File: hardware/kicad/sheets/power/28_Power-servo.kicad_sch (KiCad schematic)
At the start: 18 parts, among them U37 TPSM63610RDFR

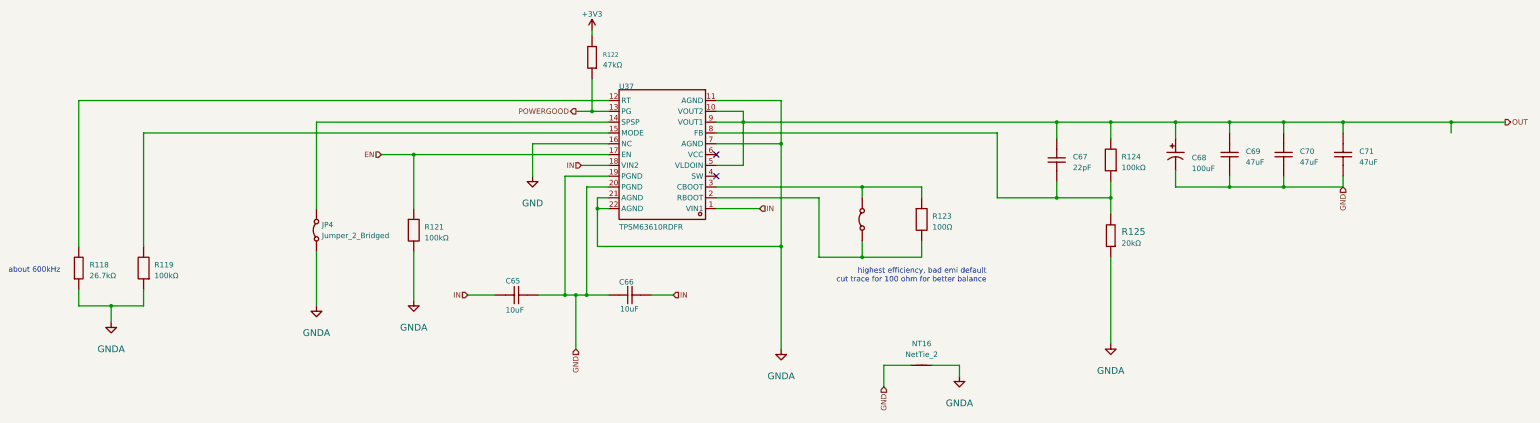
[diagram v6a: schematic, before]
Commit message: 5v usb c done, esc mostly done
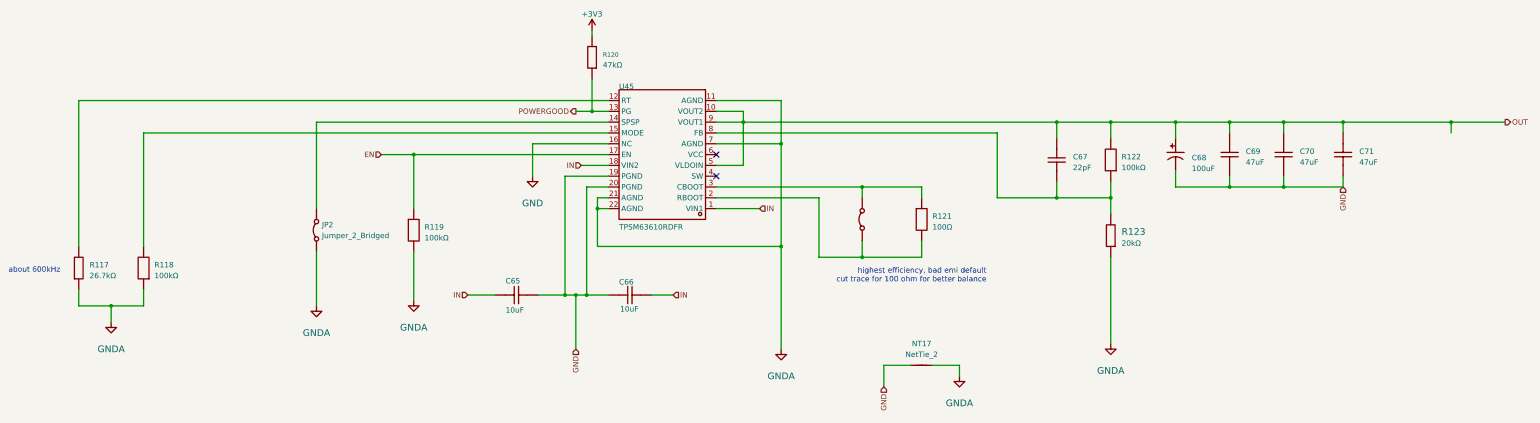
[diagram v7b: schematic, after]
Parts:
- renumbered JP4 to JP2, NT16 to NT17, R118 to R117, R119 to R118, R121 to R119, R122 to R120, R123 to R121, R124 to R122, R125 to R123, U37 to U45, U38 to U46
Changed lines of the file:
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@@
 		(dnp no)
 		(fields_autoplaced yes)
-		(property "Reference" "JP4"
+		(property "Reference" "JP2"
 			(at 93.98 109.2199 90)
 			(effects
@@
 			(project ""
 				(path "/3f85abf4-0b95-4c4a-b7e9-06f59ca1ea3d/5c2e021f-c2d4-49e2-8c36-9a64f1f12001/5e87fa27-0735-4860-928c-5f9d8795dad6"
-					(reference "JP4")
+					(reference "JP2")
 					(unit 1)
 				)
@@
 		(on_board yes)
 		(dnp no)
-		(property "Reference" "R125"
+		(property "Reference" "R123"
 			(at 281.94 111.76 90)
 			(effects
@@
 			(project "svea_powerboard_rev3"
 				(path "/3f85abf4-0b95-4c4a-b7e9-06f59ca1ea3d/5c2e021f-c2d4-49e2-8c36-9a64f1f12001/5e87fa27-0735-4860-928c-5f9d8795dad6"
-					(reference "R125")
+					(reference "R123")
 					(unit 1)
 				)
@@
 		(on_board yes)
 		(dnp no)
-		(property "Reference" "U38"
+		(property "Reference" "U46"
 			(at 220.98 107.95 90)
 			(effects
@@
 			(project "svea_powerboard_rev3"
 				(path "/3f85abf4-0b95-4c4a-b7e9-06f59ca1ea3d/5c2e021f-c2d4-49e2-8c36-9a64f1f12001/5e87fa27-0735-4860-928c-5f9d8795dad6"
-					(reference "U38")
+					(reference "U46")
 					(unit 1)
 				)
@@
 		(on_board yes)
 		(dnp no)
-		(property "Reference" "#PWR0112"
+		(property "Reference" "#PWR0110"
 			(at 243.84 144.78 0)
 			(effects
@@
 			(project "svea_powerboard_rev3"
 				(path "/3f85abf4-0b95-4c4a-b7e9-06f59ca1ea3d/5c2e021f-c2d4-49e2-8c36-9a64f1f12001/5e87fa27-0735-4860-928c-5f9d8795dad6"
-					(reference "#PWR0112")
+					(reference "#PWR0110")
 					(unit 1)
 				)
@@
 		(dnp no)
 		(fields_autoplaced yes)
-		(property "Reference" "NT16"
+		(property "Reference" "NT17"
 			(at 234.95 137.16 0)
 			(effects
@@
 			(project "svea_powerboard_rev3"
 				(path "/3f85abf4-0b95-4c4a-b7e9-06f59ca1ea3d/5c2e021f-c2d4-49e2-8c36-9a64f1f12001/5e87fa27-0735-4860-928c-5f9d8795dad6"
-					(reference "NT16")
+					(reference "NT17")
 					(unit 1)
 				)
@@
 		(on_board yes)
 		(dnp no)
-		(property "Reference" "R124"
+		(property "Reference" "R122"
 			(at 281.94 93.98 90)
 			(effects
@@
 			(project "svea_powerboard_rev3"
 				(path "/3f85abf4-0b95-4c4a-b7e9-06f59ca1ea3d/5c2e021f-c2d4-49e2-8c36-9a64f1f12001/5e87fa27-0735-4860-928c-5f9d8795dad6"
-					(reference "R124")
+					(reference "R122")
 					(unit 1)
 				)
@@
 		(on_board yes)
 		(dnp no)
-		(property "Reference" "#PWR0106"
+		(property "Reference" "#PWR0104"
 			(at 44.45 132.08 0)
 			(effects
@@
 			(project "svea_powerboard_rev3"
 				(path "/3f85abf4-0b95-4c4a-b7e9-06f59ca1ea3d/5c2e021f-c2d4-49e2-8c36-9a64f1f12001/5e87fa27-0735-4860-928c-5f9d8795dad6"
-					(reference "#PWR0106")
+					(reference "#PWR0104")
 					(unit 1)
 				)
@@
 		(on_board yes)
 		(dnp no)
-		(property "Reference" "#PWR0113"
+		(property "Reference" "#PWR0111"
 			(at 279.4 137.16 0)
 			(effects
@@
 			(project "svea_powerboard_rev3"
 				(path "/3f85abf4-0b95-4c4a-b7e9-06f59ca1ea3d/5c2e021f-c2d4-49e2-8c36-9a64f1f12001/5e87fa27-0735-4860-928c-5f9d8795dad6"
-					(reference "#PWR0113")
+					(reference "#PWR0111")
 					(unit 1)
 				)
@@
 		(on_board yes)
 		(dnp no)
-		(property "Reference" "R118"
+		(property "Reference" "R117"
 			(at 39.37 119.38 90)
 			(effects
@@
 			(project "svea_powerboard_rev3"
 				(path "/3f85abf4-0b95-4c4a-b7e9-06f59ca1ea3d/5c2e021f-c2d4-49e2-8c36-9a64f1f12001/5e87fa27-0735-4860-928c-5f9d8795dad6"
-					(reference "R118")
+					(reference "R117")
 					(unit 1)
 				)
@@
 		(on_board yes)
 		(dnp no)
-		(property "Reference" "R122"
+		(property "Reference" "R120"
 			(at 160.02 69.85 90)
 			(effects
@@
 			(project "svea_powerboard_rev3"
 				(path "/3f85abf4-0b95-4c4a-b7e9-06f59ca1ea3d/5c2e021f-c2d4-49e2-8c36-9a64f1f12001/5e87fa27-0735-4860-928c-5f9d8795dad6"
-					(reference "R122")
+					(reference "R120")
 					(unit 1)
 				)
@@
 		(on_board yes)
 		(dnp no)
-		(property "Reference" "#PWR0108"
+		(property "Reference" "#PWR0106"
 			(at 115.57 127 0)
 			(effects
@@
 			(project "svea_powerboard_rev3"
 				(path "/3f85abf4-0b95-4c4a-b7e9-06f59ca1ea3d/5c2e021f-c2d4-49e2-8c36-9a64f1f12001/5e87fa27-0735-4860-928c-5f9d8795dad6"
-					(reference "#PWR0108")
+					(reference "#PWR0106")
 					(unit 1)
 				)
@@
 		(on_board yes)
 		(dnp no)
-		(property "Reference" "R123"
+		(property "Reference" "R121"
 			(at 237.49 107.95 90)
 			(effects
@@
 			(project "svea_powerboard_rev3"
 				(path "/3f85abf4-0b95-4c4a-b7e9-06f59ca1ea3d/5c2e021f-c2d4-49e2-8c36-9a64f1f12001/5e87fa27-0735-4860-928c-5f9d8795dad6"
-					(reference "R123")
+					(reference "R121")
 					(unit 1)
 				)
@@
 		(on_board yes)
 		(dnp no)
-		(property "Reference" "#PWR0111"
+		(property "Reference" "#PWR0109"
 			(at 201.93 138.43 0)
 			(effects
@@
 			(project "svea_powerboard_rev3"
 				(path "/3f85abf4-0b95-4c4a-b7e9-06f59ca1ea3d/5c2e021f-c2d4-49e2-8c36-9a64f1f12001/5e87fa27-0735-4860-928c-5f9d8795dad6"
-					(reference "#PWR0111")
+					(reference "#PWR0109")
 					(unit 1)
 				)
@@
 		(on_board yes)
 		(dnp no)
-		(property "Reference" "R121"
+		(property "Reference" "R119"
 			(at 118.11 110.49 90)
 			(effects
@@
 			(project "svea_powerboard_rev3"
 				(path "/3f85abf4-0b95-4c4a-b7e9-06f59ca1ea3d/5c2e021f-c2d4-49e2-8c36-9a64f1f12001/5e87fa27-0735-4860-928c-5f9d8795dad6"
-					(reference "R121")
+					(reference "R119")
 					(unit 1)
 				)
@@
 		(on_board yes)
 		(dnp no)
-		(property "Reference" "#PWR0110"
+		(property "Reference" "#PWR0108"
 			(at 157.48 63.5 0)
 			(effects
@@
 			(project "svea_powerboard_rev3"
 				(path "/3f85abf4-0b95-4c4a-b7e9-06f59ca1ea3d/5c2e021f-c2d4-49e2-8c36-9a64f1f12001/5e87fa27-0735-4860-928c-5f9d8795dad6"
-					(reference "#PWR0110")
+					(reference "#PWR0108")
 					(unit 1)
 				)
@@
 		(on_board yes)
 		(dnp no)
-		(property "Reference" "#PWR0107"
+		(property "Reference" "#PWR0105"
 			(at 92.71 128.27 0)
 			(effects
@@
 			(project "svea_powerboard_rev3"
 				(path "/3f85abf4-0b95-4c4a-b7e9-06f59ca1ea3d/5c2e021f-c2d4-49e2-8c36-9a64f1f12001/5e87fa27-0735-4860-928c-5f9d8795dad6"
-					(reference "#PWR0107")
+					(reference "#PWR0105")
 					(unit 1)
 				)
@@
 		(on_board yes)
 		(dnp no)
-		(property "Reference" "U37"
+		(property "Reference" "U45"
 			(at 163.83 77.47 0)
 			(effects
@@
 			(project "svea_powerboard_rev3"
 				(path "/3f85abf4-0b95-4c4a-b7e9-06f59ca1ea3d/5c2e021f-c2d4-49e2-8c36-9a64f1f12001/5e87fa27-0735-4860-928c-5f9d8795dad6"
-					(reference "U37")
+					(reference "U45")
 					(unit 1)
 				)
@@
 		(on_board yes)
 		(dnp no)
-		(property "Reference" "R119"
+		(property "Reference" "R118"
 			(at 54.61 119.38 90)
 			(effects
@@
 			(project "svea_powerboard_rev3"
 				(path "/3f85abf4-0b95-4c4a-b7e9-06f59ca1ea3d/5c2e021f-c2d4-49e2-8c36-9a64f1f12001/5e87fa27-0735-4860-928c-5f9d8795dad6"
-					(reference "R119")
+					(reference "R118")
 					(unit 1)
 				)
@@
 		(on_board yes)
 		(dnp no)
-		(property "Reference" "#PWR0109"
+		(property "Reference" "#PWR0107"
 			(at 143.51 97.79 0)
 			(effects
@@
 			(project "svea_powerboard_rev3"
 				(path "/3f85abf4-0b95-4c4a-b7e9-06f59ca1ea3d/5c2e021f-c2d4-49e2-8c36-9a64f1f12001/5e87fa27-0735-4860-928c-5f9d8795dad6"
-					(reference "#PWR0109")
-					(unit 1)
-				)
+					(reference "#PWR0107")
+					(unit 1)
+				)

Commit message: ideal diode initial layout and some fixes
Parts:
- removed U45: TPSM63610RDFR, 5v rail sm-easyedapro:QFN-22_L7.5-W6.5_TLVM13610RDFR, symbol 5v rail sm-easyedapro:TPSM63610RDFR
- added U55: TPSM63610RDFR, JLCImport:TPSM63610RDFR, symbol JLCImport:TPSM63610RDFR
- renumbered U46 to U56
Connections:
- net EN: now also U55.17 (EN)
- net GND: now also U55.16 (NC), U55.19 (PGND), U55.20 (PGND)
- net GNDA: now also U55.11 (AGND), U55.21 (AGND), U55.22 (AGND), U55.7 (AGND)
- net IN: now also U55.1 (VIN1), U55.18 (VIN2)
- net OUT: now also U55.10 (VOUT2), U55.5 (VLDOIN), U55.9 (VOUT1)
- net POWERGOOD: now also U55.13 (PG)
- net at JP2.2 (B): now also U55.14 (SPSP)
- net at C67.1, R122.1, R123.2: now also U55.8 (FB)
- net at R121.2, U56.1 (A): now also U55.2 (RBOOT)
- net at R121.1, U56.2 (B): now also U55.3 (CBOOT)
- net at R117.2: now also U55.12 (RT)
- net at R118.2: now also U55.15 (MODE)
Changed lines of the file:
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@@
 		(on_board yes)
 		(dnp no)
-		(property "Reference" "U46"
+		(property "Reference" "U56"
 			(at 220.98 107.95 90)
 			(effects
@@
 			(project "svea_powerboard_rev3"
 				(path "/3f85abf4-0b95-4c4a-b7e9-06f59ca1ea3d/5c2e021f-c2d4-49e2-8c36-9a64f1f12001/5e87fa27-0735-4860-928c-5f9d8795dad6"
-					(reference "U46")
+					(reference "U56")
 					(unit 1)
 				)
@@
 		(on_board yes)
 		(dnp no)
-		(property "Reference" "#PWR0110"
+		(property "Reference" "#PWR0111"
 			(at 243.84 144.78 0)
 			(effects
@@
 			(project "svea_powerboard_rev3"
 				(path "/3f85abf4-0b95-4c4a-b7e9-06f59ca1ea3d/5c2e021f-c2d4-49e2-8c36-9a64f1f12001/5e87fa27-0735-4860-928c-5f9d8795dad6"
-					(reference "#PWR0110")
+					(reference "#PWR0111")
 					(unit 1)
 				)
@@
 		(on_board yes)
 		(dnp no)
-		(property "Reference" "#PWR0104"
+		(property "Reference" "#PWR0105"
 			(at 44.45 132.08 0)
 			(effects
@@
 			(project "svea_powerboard_rev3"
 				(path "/3f85abf4-0b95-4c4a-b7e9-06f59ca1ea3d/5c2e021f-c2d4-49e2-8c36-9a64f1f12001/5e87fa27-0735-4860-928c-5f9d8795dad6"
-					(reference "#PWR0104")
+					(reference "#PWR0105")
 					(unit 1)
 				)
@@
 		(on_board yes)
 		(dnp no)
-		(property "Reference" "#PWR0111"
+		(property "Reference" "#PWR0112"
 			(at 279.4 137.16 0)
 			(effects
@@
 			(project "svea_powerboard_rev3"
 				(path "/3f85abf4-0b95-4c4a-b7e9-06f59ca1ea3d/5c2e021f-c2d4-49e2-8c36-9a64f1f12001/5e87fa27-0735-4860-928c-5f9d8795dad6"
-					(reference "#PWR0111")
+					(reference "#PWR0112")
 					(unit 1)
 				)
@@
 	)
 	(symbol
+		(lib_id "JLCImport:TPSM63610RDFR")
+		(at 173.99 92.71 180)
+		(unit 1)
+		(exclude_from_sim no)
+		(in_bom yes)
+		(on_board yes)
+		(dnp no)
+		(fields_autoplaced yes)
+		(property "Reference" "U55"
+			(at 173.99 72.39 0)
+			(effects
+				(font
+					(size 1.27 1.27)
+				)
+			)
+		)
+		(property "Value" "TPSM63610RDFR"
+			(at 173.99 74.93 0)
+			(effects
+				(font
+					(size 1.27 1.27)
+				)
+			)
+		)
+		(property "Footprint" "JLCImport:TPSM63610RDFR"
+			(at 173.99 92.71 0)
+			(effects
+				(font
+					(size 1.27 1.27)
+				)
+				(hide yes)
+			)
+		)
+		(property "Datasheet" "https://www.ti.com.cn/cn/lit/ml/mpqf620/mpqf620.pdf?ts=1684740647599&ref_url=https%253A%252F%252Fwww.ti.com.cn%252Fsitesearch%252Fzh-cn%252Fdocs%252Funiversalsearch.tsp%253FlangPref%253Dzh-CN%2526searchTerm%253DTLVM13610RDFR%2526nr%253D9"
+			(at 173.99 92.71 0)
+			(effects
+				(font
+					(size 1.27 1.27)
+				)
+				(hide yes)
+			)
+		)
+		(property "Description" ""
+			(at 173.99 92.71 0)
+			(effects
+				(font
+					(size 1.27 1.27)
+				)
+				(hide yes)
+			)
+		)
+		(property "LCSC" "C7125816"
+			(at 173.99 92.71 0)
+			(effects
+				(font
+					(size 1.27 1.27)
+				)
+				(hide yes)
+			)
+		)
+		(property "Manufacturer" "TI(德州仪器)"
+			(at 173.99 92.71 0)
+			(effects
+				(font
+					(size 1.27 1.27)
+				)
+				(hide yes)
+			)
+		)
+		(property "Manufacturer Part" "TPSM63610RDFR"
+			(at 173.99 92.71 0)
+			(effects
+				(font
+					(size 1.27 1.27)
+				)
+				(hide yes)
+			)
+		)
+		(pin "13"
+		)
+		(pin "12"
+		)
+		(pin "15"
+		)
+		(pin "14"
+		)
+		(pin "16"
+		)
+		(pin "17"
+		)
+		(pin "18"
+		)
+		(pin "19"
+		)
+		(pin "20"
+		)
+		(pin "21"
+		)
+		(pin "22"
+		)
+		(pin "11"
+		)
+		(pin "10"
+		)
+		(pin "9"
+		)
+		(pin "8"
+		)
+		(pin "7"
+		)
+		(pin "6"
+		)
+		(pin "5"
+		)
+		(pin "4"
+		)
+		(pin "3"
+		)
+		(pin "2"
+		)
+		(pin "1"
+		)
+		(instances
+			(project ""
+				(path "/3f85abf4-0b95-4c4a-b7e9-06f59ca1ea3d/5c2e021f-c2d4-49e2-8c36-9a64f1f12001/5e87fa27-0735-4860-928c-5f9d8795dad6"
+					(reference "U55")
+					(unit 1)
+				)
+			)
+		)
+	)
+	(symbol
 		(lib_id "5v rail sm-easyedapro:0603WAF4702T5E")
 		(at 157.48 69.85 90)
@@
 		(on_board yes)
 		(dnp no)
-		(property "Reference" "#PWR0106"
+		(property "Reference" "#PWR0107"
 			(at 115.57 127 0)
 			(effects
@@
 			(project "svea_powerboard_rev3"
 				(path "/3f85abf4-0b95-4c4a-b7e9-06f59ca1ea3d/5c2e021f-c2d4-49e2-8c36-9a64f1f12001/5e87fa27-0735-4860-928c-5f9d8795dad6"
-					(reference "#PWR0106")
+					(reference "#PWR0107")
 					(unit 1)
 				)
@@
 		(on_board yes)
 		(dnp no)
-		(property "Reference" "#PWR0109"
+		(property "Reference" "#PWR0110"
 			(at 201.93 138.43 0)
 			(effects
@@
 			(project "svea_powerboard_rev3"
 				(path "/3f85abf4-0b95-4c4a-b7e9-06f59ca1ea3d/5c2e021f-c2d4-49e2-8c36-9a64f1f12001/5e87fa27-0735-4860-928c-5f9d8795dad6"
-					(reference "#PWR0109")
+					(reference "#PWR0110")
 					(unit 1)
 				)
@@
 		(on_board yes)
 		(dnp no)
-		(property "Reference" "#PWR0108"
+		(property "Reference" "#PWR0109"
 			(at 157.48 63.5 0)
 			(effects
@@
 			(project "svea_powerboard_rev3"
 				(path "/3f85abf4-0b95-4c4a-b7e9-06f59ca1ea3d/5c2e021f-c2d4-49e2-8c36-9a64f1f12001/5e87fa27-0735-4860-928c-5f9d8795dad6"
-					(reference "#PWR0108")
+					(reference "#PWR0109")
 					(unit 1)
 				)
@@
 		(on_board yes)
 		(dnp no)
-		(property "Reference" "#PWR0105"
+		(property "Reference" "#PWR0106"
 			(at 92.71 128.27 0)
 			(effects
@@
 			(project "svea_powerboard_rev3"
 				(path "/3f85abf4-0b95-4c4a-b7e9-06f59ca1ea3d/5c2e021f-c2d4-49e2-8c36-9a64f1f12001/5e87fa27-0735-4860-928c-5f9d8795dad6"
-					(reference "#PWR0105")
-					(unit 1)
-				)
-			)
-		)
-	)
-	(symbol
-		(lib_id "5v rail sm-easyedapro:TPSM63610RDFR")
-		(at 173.99 92.71 180)
-		(unit 1)
-		(exclude_from_sim no)
-		(in_bom yes)
-		(on_board yes)
-		(dnp no)
-		(property "Reference" "U45"
-			(at 163.83 77.47 0)
-			(effects
-				(font
-					(size 1.27 1.27)
-				)
-				(justify right top)
-			)
-		)
-		(property "Value" "TPSM63610RDFR"
-			(at 163.83 110.49 0)
-			(effects
-				(font
-					(size 1.27 1.27)
-				)
-				(justify right top)
-			)
-		)
-		(property "Footprint" "5v rail sm-easyedapro:QFN-22_L7.5-W6.5_TLVM13610RDFR"
-			(at 173.99 92.71 0)
-			(effects
-				(font
-					(size 1.27 1.27)
-				)
-				(hide yes)
-			)
-		)
-		(property "Datasheet" "https://item.szlcsc.com/datasheet/TPSM63610RDFR/8092608.html"
-			(at 173.99 92.71 0)
-			(effects
-				(font
-					(size 1.27 1.27)
-				)
-				(hide yes)
-			)
-		)
-		(property "Description" "Function:Buck Number of Outputs:1 Voltage - Supply:3V~36V Voltage - Supply:3V~36V Output Voltage Accuracy:±1% Output Voltage Accuracy:±1% Output Voltage:1V~20V Output Voltage:1V~20V Output Current(Max):8A Output Current(Max):8A Conversion Efficiency:95% C"
-			(at 173.99 92.71 0)
-			(effects
-				(font
-					(size 1.27 1.27)
-				)
-				(hide yes)
-			)
-		)
-		(property "Manufacturer Part" "TPSM63610RDFR"
-			(at 173.99 92.71 0)
-			(effects
-				(font
-					(size 1.27 1.27)
-				)
-				(hide yes)
-			)
-		)
-		(property "Manufacturer" "TI(德州仪器)"
-			(at 173.99 92.71 0)
-			(effects
-				(font
-					(size 1.27 1.27)
-				)
-				(hide yes)
-			)
-		)
-		(property "Supplier Part" "C7125816"
-			(at 173.99 92.71 0)
-			(effects
-				(font
-					(size 1.27 1.27)
-				)
-				(hide yes)
-			)
-		)
-		(property "Supplier" "LCSC"
-			(at 173.99 92.71 0)
-			(effects
-				(font
-					(size 1.27 1.27)
-				)
-				(hide yes)
-			)
-		)
-		(property "LCSC Part Name" "TPSM63610RDFR"
-			(at 173.99 92.71 0)
-			(effects
-				(font
-					(size 1.27 1.27)
-				)
-				(hide yes)
-			)
-		)
-		(pin "1"
-		)
-		(pin "2"
-		)
-		(pin "3"
-		)
-		(pin "4"
-		)
-		(pin "5"
-		)
-		(pin "6"
-		)
-		(pin "7"
-		)
-		(pin "8"
-		)
-		(pin "9"
-		)
-		(pin "10"
-		)
-		(pin "11"
-		)
-		(pin "22"
-		)
-		(pin "21"
-		)
-		(pin "20"
-		)
-		(pin "19"
-		)
-		(pin "18"
-		)
-		(pin "17"
-		)
-		(pin "16"
-		)
-		(pin "15"
-		)
-		(pin "14"
-		)
-		(pin "13"
-		)
-		(pin "12"
-		)
-		(instances
-			(project "svea_powerboard_rev3"
-				(path "/3f85abf4-0b95-4c4a-b7e9-06f59ca1ea3d/5c2e021f-c2d4-49e2-8c36-9a64f1f12001/5e87fa27-0735-4860-928c-5f9d8795dad6"
-					(reference "U45")
+					(reference "#PWR0106")
 					(unit 1)
 				)
@@
 		(on_board yes)
 		(dnp no)
-		(property "Reference" "#PWR0107"
+		(property "Reference" "#PWR0108"
 			(at 143.51 97.79 0)
 			(effects
@@
 			(project "svea_powerboard_rev3"
 				(path "/3f85abf4-0b95-4c4a-b7e9-06f59ca1ea3d/5c2e021f-c2d4-49e2-8c36-9a64f1f12001/5e87fa27-0735-4860-928c-5f9d8795dad6"
-					(reference "#PWR0107")
-					(unit 1)
-				)
+					(reference "#PWR0108")
+					(unit 1)
+				)
